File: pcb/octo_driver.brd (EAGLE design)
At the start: 34.3 x 46.2 mm, 16 parts

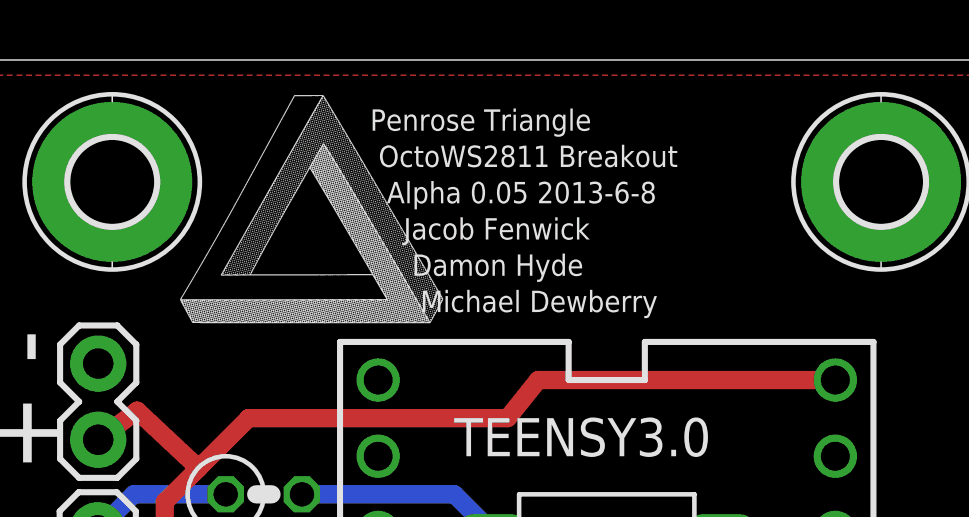
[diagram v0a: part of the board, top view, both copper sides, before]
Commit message: Nudge PCB logo a bit; add Eagle .gitignore
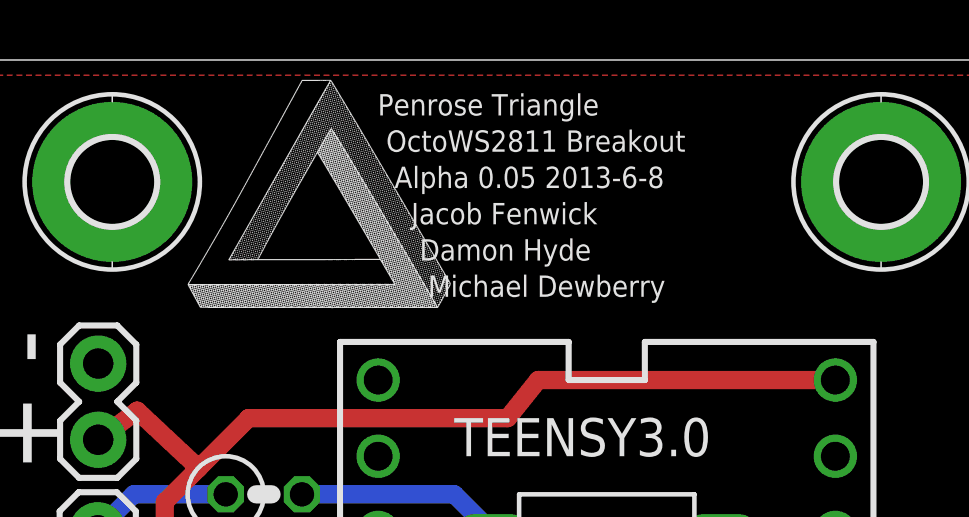
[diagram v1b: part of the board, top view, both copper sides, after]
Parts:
- moved E$1 0.57 mm to (53.9, 49.0)
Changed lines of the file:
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@@
 <?xml version="1.0" encoding="utf-8"?>
 <!DOCTYPE eagle SYSTEM "eagle.dtd">
-<eagle version="6.3">
+<eagle version="6.4">
 <drawing>
 <settings>
@@
 <wire x1="76.708" y1="7.62" x2="42.418" y2="7.62" width="0" layer="20"/>
 <wire x1="42.418" y1="7.62" x2="42.418" y2="53.848" width="0" layer="20"/>
-<text x="55.610759375" y="45.44568125" size="0.7112" layer="25" font="vector" ratio="15" distance="70">Penrose Triangle
+<text x="55.864759375" y="45.95368125" size="0.7112" layer="25" font="vector" ratio="15" distance="70">Penrose Triangle
  OctoWS2811 Breakout
   Alpha 0.05 2013-6-8
@@
 <element name="H2" library="holes" package="2,8-PAD" value="MOUNT-PAD-ROUND2.8" x="47.016" y="49.784"/>
 <element name="H3" library="holes" package="2,8-PAD" value="MOUNT-PAD-ROUND2.8" x="72.644" y="49.784"/>
-<element name="E$1" library="penrose" package="PENROSELOGO" value="" x="53.67528125" y="48.516540625"/>
+<element name="E$1" library="penrose" package="PENROSELOGO" value="" x="53.92928125" y="49.024540625"/>
 </elements>
 <signals>

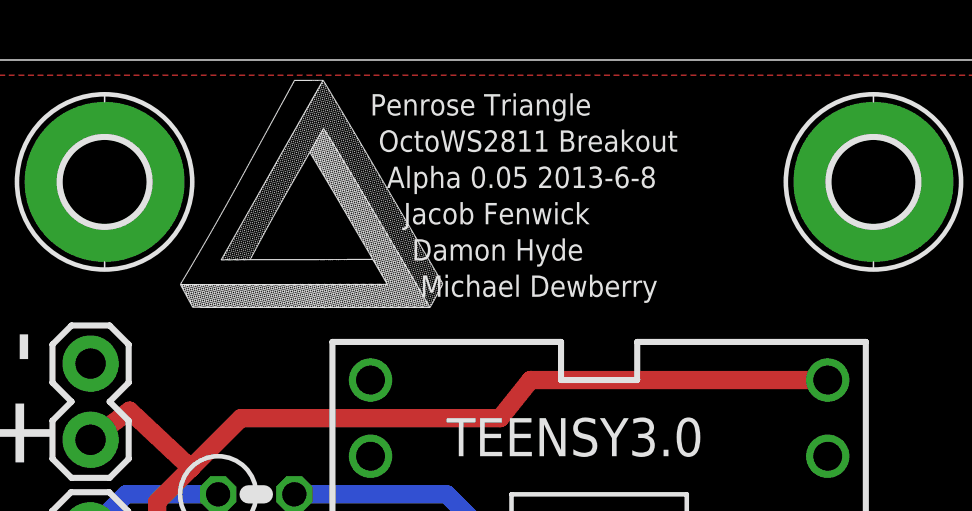
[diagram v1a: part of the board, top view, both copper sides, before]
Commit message: Lower DPI logo
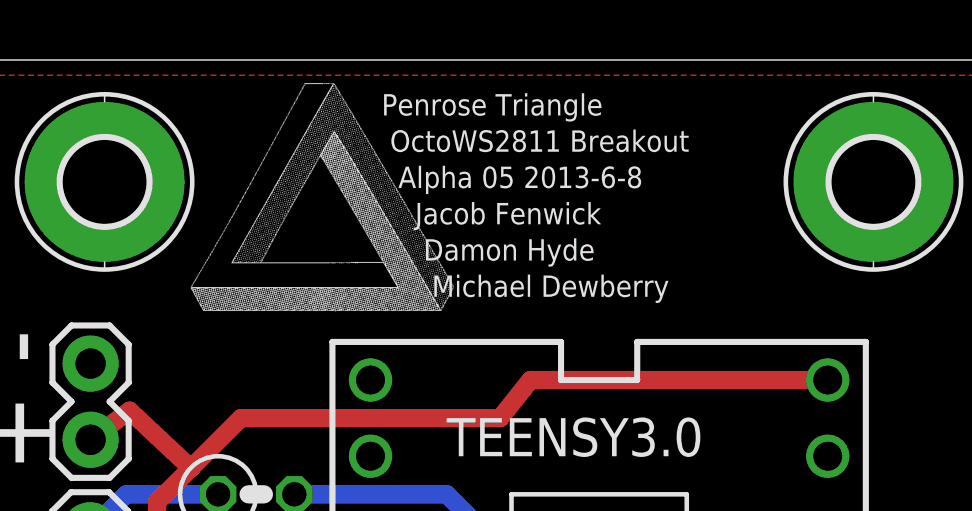
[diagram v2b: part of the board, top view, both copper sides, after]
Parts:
- moved E$1 0.40 mm to (54.1, 48.6)
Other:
- board text added: "Penrose Triangle OctoWS2811 Breakout Alpha 05 2013-6-8 Jacob Fenwick Damon Hyde Michael Dewberry"
- board text removed: "Penrose Triangle OctoWS2811 Breakout Alpha 0.05 2013-6-8 Jacob Fenwick Damon Hyde Michael Dewberry"
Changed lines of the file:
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@@
 <wire x1="76.708" y1="7.62" x2="42.418" y2="7.62" width="0" layer="20"/>
 <wire x1="42.418" y1="7.62" x2="42.418" y2="53.848" width="0" layer="20"/>
-<text x="55.864759375" y="45.95368125" size="0.7112" layer="25" font="vector" ratio="15" distance="70">Penrose Triangle
+<text x="56.245759375" y="45.95368125" size="0.7112" layer="25" font="vector" ratio="15" distance="70">Penrose Triangle
  OctoWS2811 Breakout
-  Alpha 0.05 2013-6-8
+  Alpha 05 2013-6-8
     Jacob Fenwick
      Damon Hyde
@@
 <element name="H2" library="holes" package="2,8-PAD" value="MOUNT-PAD-ROUND2.8" x="47.016" y="49.784"/>
 <element name="H3" library="holes" package="2,8-PAD" value="MOUNT-PAD-ROUND2.8" x="72.644" y="49.784"/>
-<element name="E$1" library="penrose" package="PENROSELOGO" value="" x="53.92928125" y="49.024540625"/>
+<element name="E$1" library="penrose" package="PENROSELOGO" value="" x="54.05628125" y="48.643540625"/>
 </elements>
 <signals>

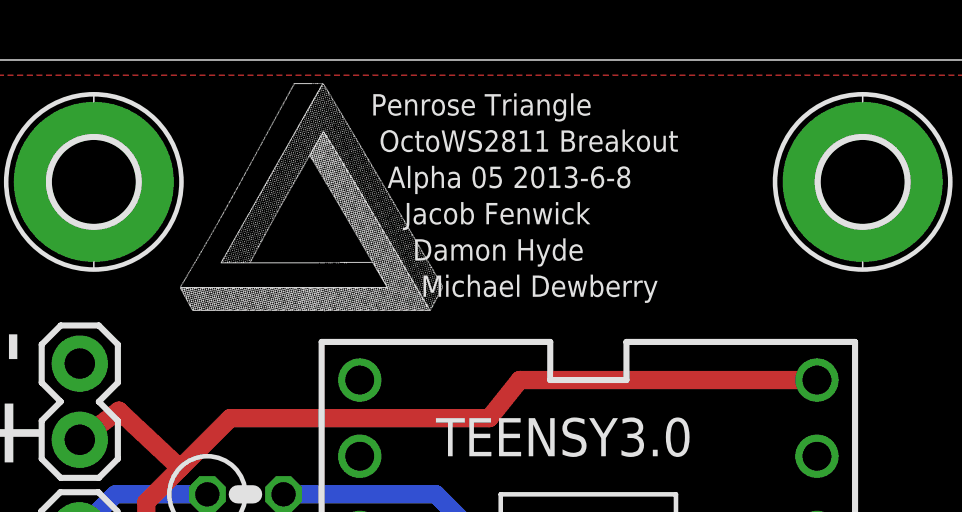
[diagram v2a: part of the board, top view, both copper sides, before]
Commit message: Even lower res logo, 200dpi for OSHPark
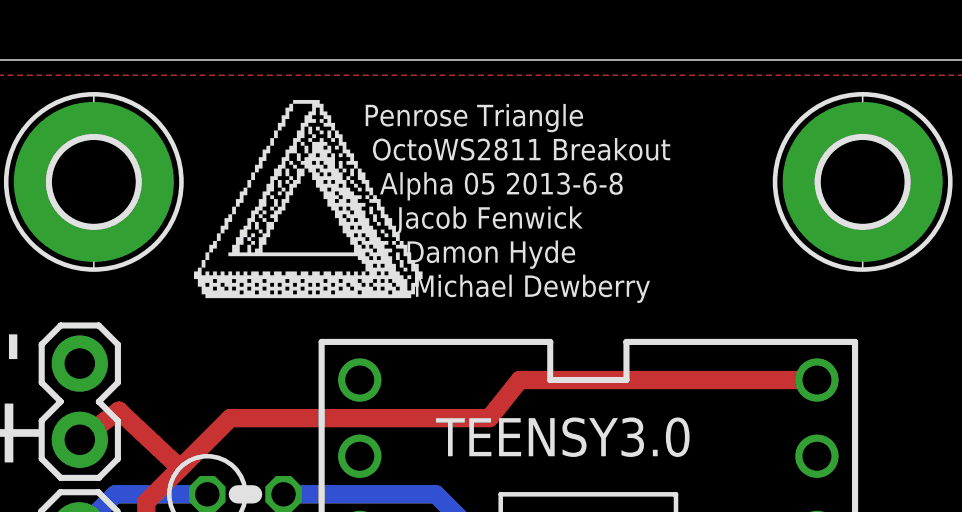
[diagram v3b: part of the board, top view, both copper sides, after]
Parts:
- E$1: device penrose:PENROSELOGO -> penrose:PENROSELOGO_LOWDPI
- moved E$1 0.39 mm to (54.1, 48.3)
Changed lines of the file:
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@@
 <wire x1="76.708" y1="7.62" x2="42.418" y2="7.62" width="0" layer="20"/>
 <wire x1="42.418" y1="7.62" x2="42.418" y2="53.848" width="0" layer="20"/>
-<text x="56.245759375" y="45.95368125" size="0.7112" layer="25" font="vector" ratio="15" distance="70">Penrose Triangle
+<text x="55.991759375" y="45.95368125" size="0.7112" layer="25" font="vector" ratio="15" distance="60">Penrose Triangle
  OctoWS2811 Breakout
   Alpha 05 2013-6-8
@@
 <element name="H2" library="holes" package="2,8-PAD" value="MOUNT-PAD-ROUND2.8" x="47.016" y="49.784"/>
 <element name="H3" library="holes" package="2,8-PAD" value="MOUNT-PAD-ROUND2.8" x="72.644" y="49.784"/>
-<element name="E$1" library="penrose" package="PENROSELOGO" value="" x="54.05628125" y="48.643540625"/>
+<element name="E$1" library="penrose" package="PENROSELOGO_LOWDPI" value="" x="54.102" y="48.26"/>
 </elements>
 <signals>
